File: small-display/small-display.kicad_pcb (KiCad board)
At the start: 4 copper layers, 43 x 62 mm, 46 parts, among them J1 2047110001, J2 Micro_SD_Card_Det, J5 F32D-1A7Y1-21040, U1 TPD4EUSB30, U2 74LVC1G07SE-7, U3 RT9742GGJ5, U4 PAM2804AAB010, U5 USB2412-DZK, U6 NLVVHC1G04DFT1G, U7 M24M01-DFDW6TP, Y1 ECS-240-8-33-AGN-TR

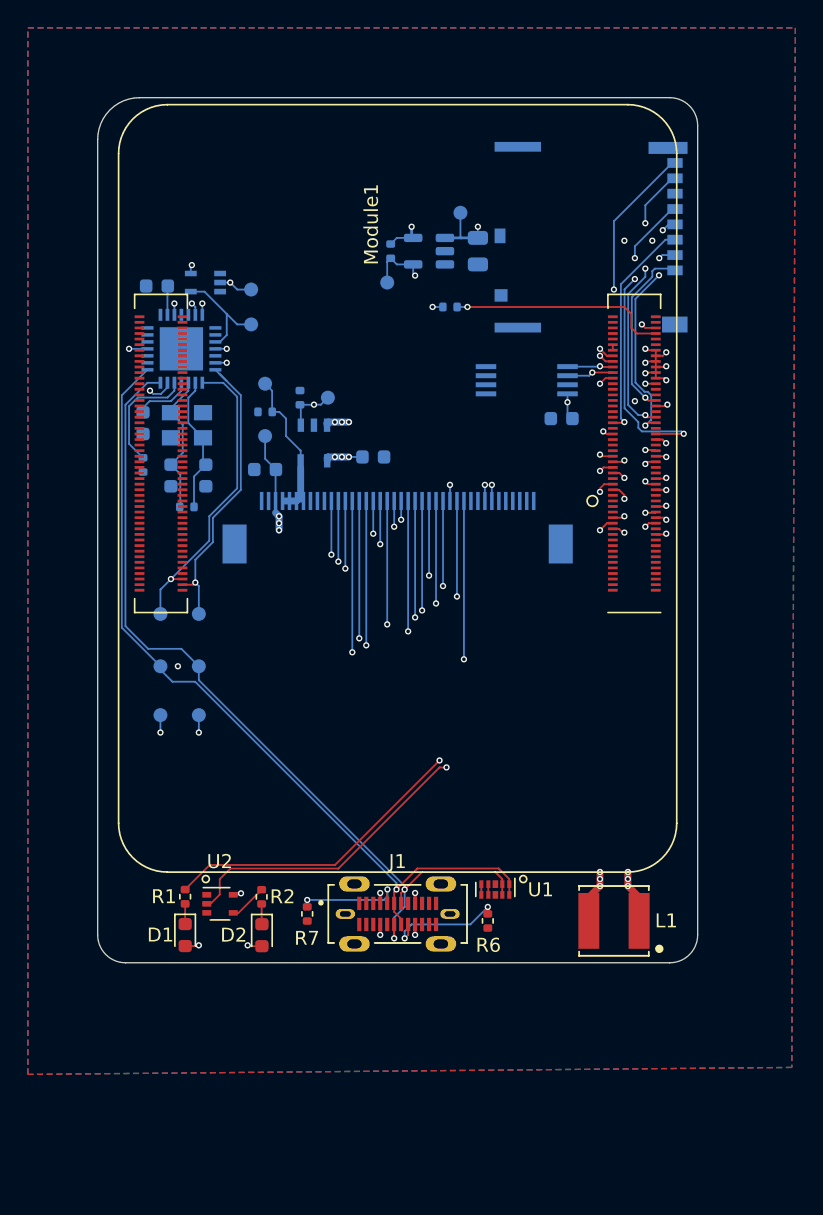
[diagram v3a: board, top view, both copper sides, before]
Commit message: Finished DRC.
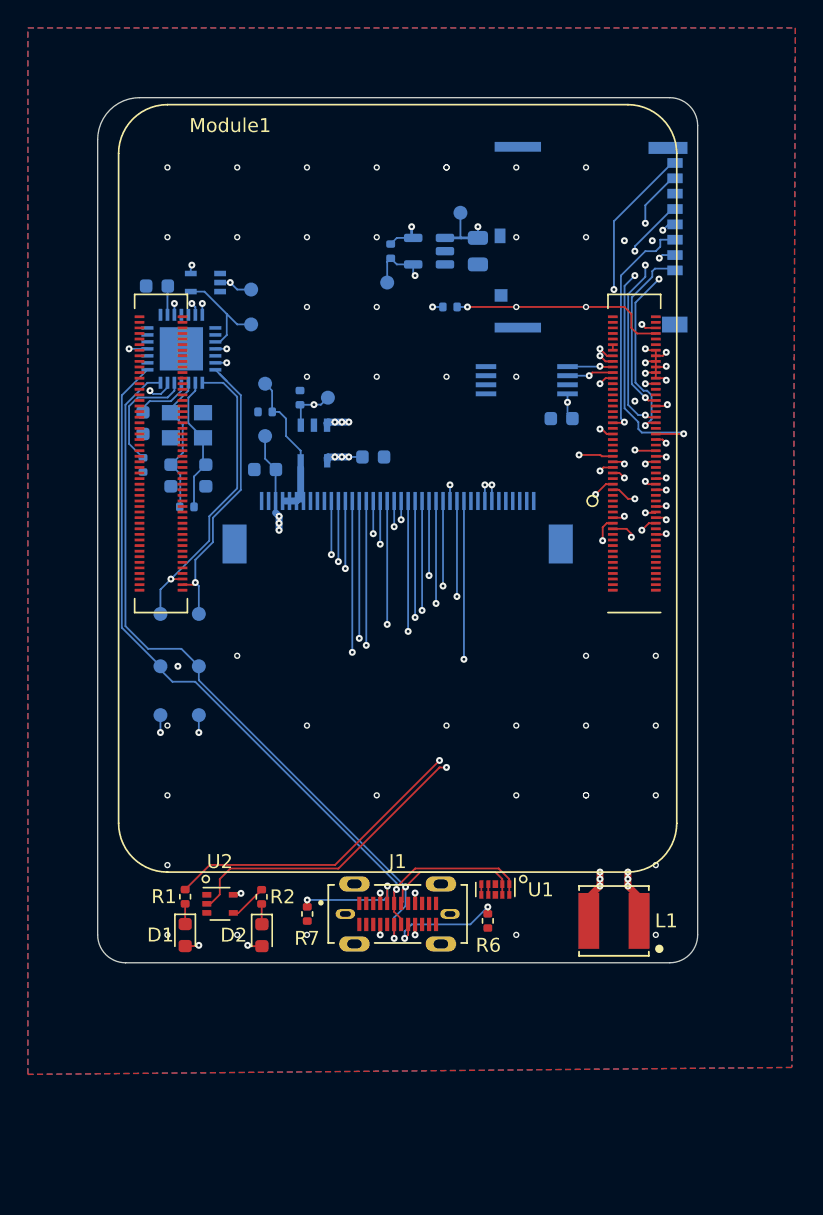
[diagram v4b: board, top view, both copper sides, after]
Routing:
- net /LED_A: track 51.3 -> 49.3 mm
- net GPIO_11_DB3: track 26.9 -> 28.3 mm
- net GPIO_26_DAT_CMD: track 27.5 -> 28.7 mm
- net SD_CMD: track 16.0 -> 16.7 mm
- net GPIO_19_DB11: track 31.6 -> 32.2 mm
- net GND: vias 5 -> 47
- net /nRPIBOOT: vias 1 -> 3
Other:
- board text added: "FPC extent"
- board text removed: "FPC"

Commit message: Ran DRC again and updated production outputs.
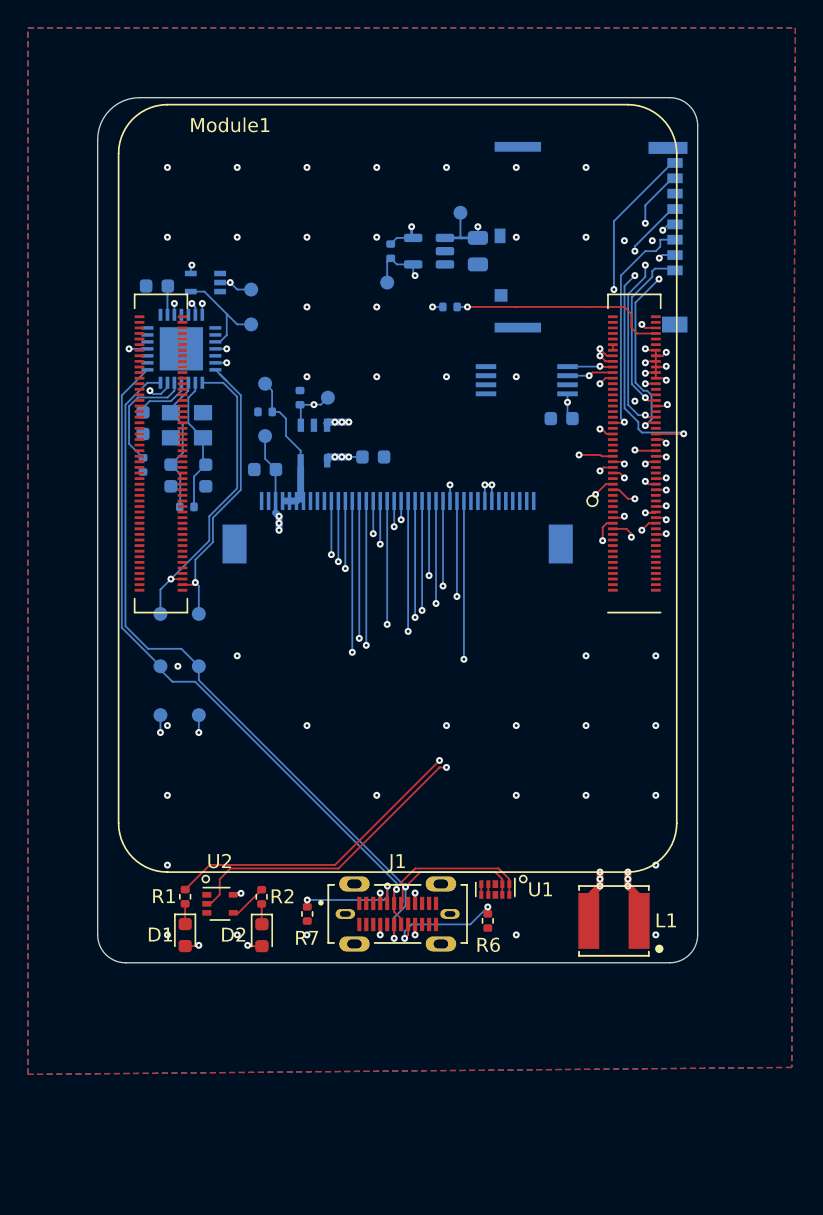
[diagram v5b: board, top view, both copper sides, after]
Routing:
- net GND: vias 47 -> 45
- net /nRPIBOOT: vias 3 -> 1
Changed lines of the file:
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@@
   (segment (start 35.974979 19.275021) (end 33.671 19.275021) (width 0.13) (layer "B.Cu") (net 22))
   (via (at 6.75 14.75) (size 0.5) (drill 0.2) (layers "F.Cu" "B.Cu") (remove_unused_layers) (net 25))
-  (via (at 25 5) (size 0.45) (drill 0.25) (layers "F.Cu" "B.Cu") (free) (net 25))
-  (via (at 40 55) (size 0.45) (drill 0.25) (layers "F.Cu" "B.Cu") (free) (net 25))
-  (via (at 10 40) (size 0.45) (drill 0.25) (layers "F.Cu" "B.Cu") (free) (net 25))
-  (via (at 5 55) (size 0.45) (drill 0.25) (layers "F.Cu" "B.Cu") (free) (net 25))
-  (via (at 40 60) (size 0.45) (drill 0.25) (layers "F.Cu" "B.Cu") (free) (net 25))
-  (via (at 25 45) (size 0.45) (drill 0.25) (layers "F.Cu" "B.Cu") (free) (net 25))
-  (via (at 15 15) (size 0.45) (drill 0.25) (layers "F.Cu" "B.Cu") (free) (net 25))
-  (via (at 40 50) (size 0.45) (drill 0.25) (layers "F.Cu" "B.Cu") (free) (net 25))
-  (via (at 35 50) (size 0.45) (drill 0.25) (layers "F.Cu" "B.Cu") (free) (net 25))
-  (via (at 5 60) (size 0.45) (drill 0.25) (layers "F.Cu" "B.Cu") (free) (net 25))
-  (via (at 30 5) (size 0.45) (drill 0.25) (layers "F.Cu" "B.Cu") (free) (net 25))
-  (via (at 15 10) (size 0.45) (drill 0.25) (layers "F.Cu" "B.Cu") (free) (net 25))
-  (via (at 20 50) (size 0.45) (drill 0.25) (layers "F.Cu" "B.Cu") (free) (net 25))
+  (via (at 40 55) (size 0.5) (drill 0.2) (layers "F.Cu" "B.Cu") (free) (net 25))
+  (via (at 10 40) (size 0.5) (drill 0.2) (layers "F.Cu" "B.Cu") (free) (net 25))
+  (via (at 5 55) (size 0.5) (drill 0.2) (layers "F.Cu" "B.Cu") (free) (net 25))
+  (via (at 40 60) (size 0.5) (drill 0.2) (layers "F.Cu" "B.Cu") (free) (net 25))
+  (via (at 25 45) (size 0.5) (drill 0.2) (layers "F.Cu" "B.Cu") (free) (net 25))
+  (via (at 15 15) (size 0.5) (drill 0.2) (layers "F.Cu" "B.Cu") (free) (net 25))
+  (via (at 40 50) (size 0.5) (drill 0.2) (layers "F.Cu" "B.Cu") (free) (net 25))
+  (via (at 5 60) (size 0.5) (drill 0.2) (layers "F.Cu" "B.Cu") (free) (net 25))
+  (via (at 30 5) (size 0.5) (drill 0.2) (layers "F.Cu" "B.Cu") (free) (net 25))
+  (via (at 15 10) (size 0.5) (drill 0.2) (layers "F.Cu" "B.Cu") (free) (net 25))
+  (via (at 20 50) (size 0.5) (drill 0.2) (layers "F.Cu" "B.Cu") (free) (net 25))
   (via (at 37.75 10.25) (size 0.5) (drill 0.2) (layers "F.Cu" "B.Cu") (remove_unused_layers) (free) (net 25))
-  (via (at 30 45) (size 0.45) (drill 0.25) (layers "F.Cu" "B.Cu") (free) (net 25))
-  (via (at 5 50) (size 0.45) (drill 0.25) (layers "F.Cu" "B.Cu") (free) (net 25))
-  (via (at 35 50) (size 0.45) (drill 0.25) (layers "F.Cu" "B.Cu") (free) (net 25))
-  (via (at 5 5) (size 0.45) (drill 0.25) (layers "F.Cu" "B.Cu") (free) (net 25))
+  (via (at 30 45) (size 0.5) (drill 0.2) (layers "F.Cu" "B.Cu") (free) (net 25))
+  (via (at 5 50) (size 0.5) (drill 0.2) (layers "F.Cu" "B.Cu") (free) (net 25))
+  (via (at 35 50) (size 0.5) (drill 0.2) (layers "F.Cu" "B.Cu") (free) (net 25))
+  (via (at 5 5) (size 0.5) (drill 0.2) (layers "F.Cu" "B.Cu") (free) (net 25))
   (via (at 5.75 40.75) (size 0.5) (drill 0.2) (layers "F.Cu" "B.Cu") (remove_unused_layers) (free) (net 25))
-  (via (at 30 10) (size 0.45) (drill 0.25) (layers "F.Cu" "B.Cu") (free) (net 25))
-  (via (at 20 15) (size 0.45) (drill 0.25) (layers "F.Cu" "B.Cu") (free) (net 25))
-  (via (at 15 5) (size 0.45) (drill 0.25) (layers "F.Cu" "B.Cu") (free) (net 25))
-  (via (at 20 5) (size 0.45) (drill 0.25) (layers "F.Cu" "B.Cu") (free) (net 25))
-  (via (at 40 45) (size 0.45) (drill 0.25) (layers "F.Cu" "B.Cu") (free) (net 25))
-  (via (at 10 10) (size 0.45) (drill 0.25) (layers "F.Cu" "B.Cu") (free) (net 25))
+  (via (at 30 10) (size 0.5) (drill 0.2) (layers "F.Cu" "B.Cu") (free) (net 25))
+  (via (at 20 15) (size 0.5) (drill 0.2) (layers "F.Cu" "B.Cu") (free) (net 25))
+  (via (at 15 5) (size 0.5) (drill 0.2) (layers "F.Cu" "B.Cu") (free) (net 25))
+  (via (at 20 5) (size 0.5) (drill 0.2) (layers "F.Cu" "B.Cu") (free) (net 25))
+  (via (at 40 45) (size 0.5) (drill 0.2) (layers "F.Cu" "B.Cu") (free) (net 25))
+  (via (at 10 10) (size 0.5) (drill 0.2) (layers "F.Cu" "B.Cu") (free) (net 25))
   (via (at 38.5 21.75) (size 0.5) (drill 0.2) (layers "F.Cu" "B.Cu") (remove_unused_layers) (free) (net 25))
-  (via (at 35 10) (size 0.45) (drill 0.25) (layers "F.Cu" "B.Cu") (free) (net 25))
-  (via (at 20 20) (size 0.45) (drill 0.25) (layers "F.Cu" "B.Cu") (free) (net 25))
-  (via (at 15 20) (size 0.45) (drill 0.25) (layers "F.Cu" "B.Cu") (free) (net 25))
-  (via (at 15 45) (size 0.45) (drill 0.25) (layers "F.Cu" "B.Cu") (free) (net 25))
-  (via (at 40 40) (size 0.45) (drill 0.25) (layers "F.Cu" "B.Cu") (free) (net 25))
-  (via (at 30 20) (size 0.45) (drill 0.25) (layers "F.Cu" "B.Cu") (free) (net 25))
-  (via (at 10 5) (size 0.45) (drill 0.25) (layers "F.Cu" "B.Cu") (free) (net 25))
-  (via (at 10 60) (size 0.45) (drill 0.25) (layers "F.Cu" "B.Cu") (free) (net 25))
-  (via (at 25 20) (size 0.45) (drill 0.25) (layers "F.Cu" "B.Cu") (free) (net 25))
-  (via (at 20 10) (size 0.45) (drill 0.25) (layers "F.Cu" "B.Cu") (free) (net 25))
-  (via (at 15 60) (size 0.45) (drill 0.25) (layers "F.Cu" "B.Cu") (free) (net 25))
-  (via (at 30 50) (size 0.45) (drill 0.25) (layers "F.Cu" "B.Cu") (free) (net 25))
+  (via (at 35 10) (size 0.5) (drill 0.2) (layers "F.Cu" "B.Cu") (free) (net 25))
+  (via (at 20 20) (size 0.5) (drill 0.2) (layers "F.Cu" "B.Cu") (free) (net 25))
+  (via (at 15 20) (size 0.5) (drill 0.2) (layers "F.Cu" "B.Cu") (free) (net 25))
+  (via (at 15 45) (size 0.5) (drill 0.2) (layers "F.Cu" "B.Cu") (free) (net 25))
+  (via (at 40 40) (size 0.5) (drill 0.2) (layers "F.Cu" "B.Cu") (free) (net 25))
+  (via (at 30 20) (size 0.5) (drill 0.2) (layers "F.Cu" "B.Cu") (free) (net 25))
+  (via (at 10 5) (size 0.5) (drill 0.2) (layers "F.Cu" "B.Cu") (free) (net 25))
+  (via (at 10 60) (size 0.5) (drill 0.2) (layers "F.Cu" "B.Cu") (free) (net 25))
+  (via (at 25 20) (size 0.5) (drill 0.2) (layers "F.Cu" "B.Cu") (free) (net 25))
+  (via (at 20 10) (size 0.5) (drill 0.2) (layers "F.Cu" "B.Cu") (free) (net 25))
+  (via (at 15 60) (size 0.5) (drill 0.2) (layers "F.Cu" "B.Cu") (free) (net 25))
+  (via (at 30 50) (size 0.5) (drill 0.2) (layers "F.Cu" "B.Cu") (free) (net 25))
   (via (at 39.75 10.25) (size 0.5) (drill 0.2) (layers "F.Cu" "B.Cu") (remove_unused_layers) (free) (net 25))
-  (via (at 5 10) (size 0.45) (drill 0.25) (layers "F.Cu" "B.Cu") (free) (net 25))
-  (via (at 35 40) (size 0.45) (drill 0.25) (layers "F.Cu" "B.Cu") (free) (net 25))
-  (via (at 35 5) (size 0.45) (drill 0.25) (layers "F.Cu" "B.Cu") (free) (net 25))
-  (via (at 25 5) (size 0.45) (drill 0.25) (layers "F.Cu" "B.Cu") (free) (net 25))
-  (via (at 30 60) (size 0.45) (drill 0.25) (layers "F.Cu" "B.Cu") (free) (net 25))
-  (via (at 35 45) (size 0.45) (drill 0.25) (layers "F.Cu" "B.Cu") (free) (net 25))
-  (via (at 5 45) (size 0.45) (drill 0.25) (layers "F.Cu" "B.Cu") (free) (net 25))
+  (via (at 5 10) (size 0.5) (drill 0.2) (layers "F.Cu" "B.Cu") (free) (net 25))
+  (via (at 35 40) (size 0.5) (drill 0.2) (layers "F.Cu" "B.Cu") (free) (net 25))
+  (via (at 35 5) (size 0.5) (drill 0.2) (layers "F.Cu" "B.Cu") (free) (net 25))
+  (via (at 25 5) (size 0.5) (drill 0.2) (layers "F.Cu" "B.Cu") (free) (net 25))
+  (via (at 30 60) (size 0.5) (drill 0.2) (layers "F.Cu" "B.Cu") (free) (net 25))
+  (via (at 35 45) (size 0.5) (drill 0.2) (layers "F.Cu" "B.Cu") (free) (net 25))
+  (via (at 5 45) (size 0.5) (drill 0.2) (layers "F.Cu" "B.Cu") (free) (net 25))
   (segment (start 7 15.565) (end 7 15) (width 0.13) (layer "B.Cu") (net 25))
   (segment (start 7 15) (end 6.75 14.75) (width 0.13) (layer "B.Cu") (net 25))
@@
   (segment (start 35 15) (end 30 15) (width 0.13) (layer "F.Cu") (net 191))
   (segment (start 37.75 15) (end 35 15) (width 0.13) (layer "F.Cu") (net 191))
-  (via (at 30 15) (size 0.45) (drill 0.25) (layers "F.Cu" "B.Cu") (net 191))
-  (via (at 35 15) (size 0.45) (drill 0.25) (layers "F.Cu" "B.Cu") (net 191))
   (via (at 26.5 15) (size 0.5) (drill 0.2) (layers "F.Cu" "B.Cu") (remove_unused_layers) (net 191))
   (segment (start 26.5 15) (end 25.76 15) (width 0.13) (layer "B.Cu") (net 191))
